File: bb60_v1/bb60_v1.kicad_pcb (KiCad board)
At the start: 2 copper layers, 141 parts, among them J1 Conn_01x04, SW1 SW_Push, SW2 SW_Push, U1 STM32F072CBTx, U2 XC6206PxxxMR, U3 USBLC6-2SC6

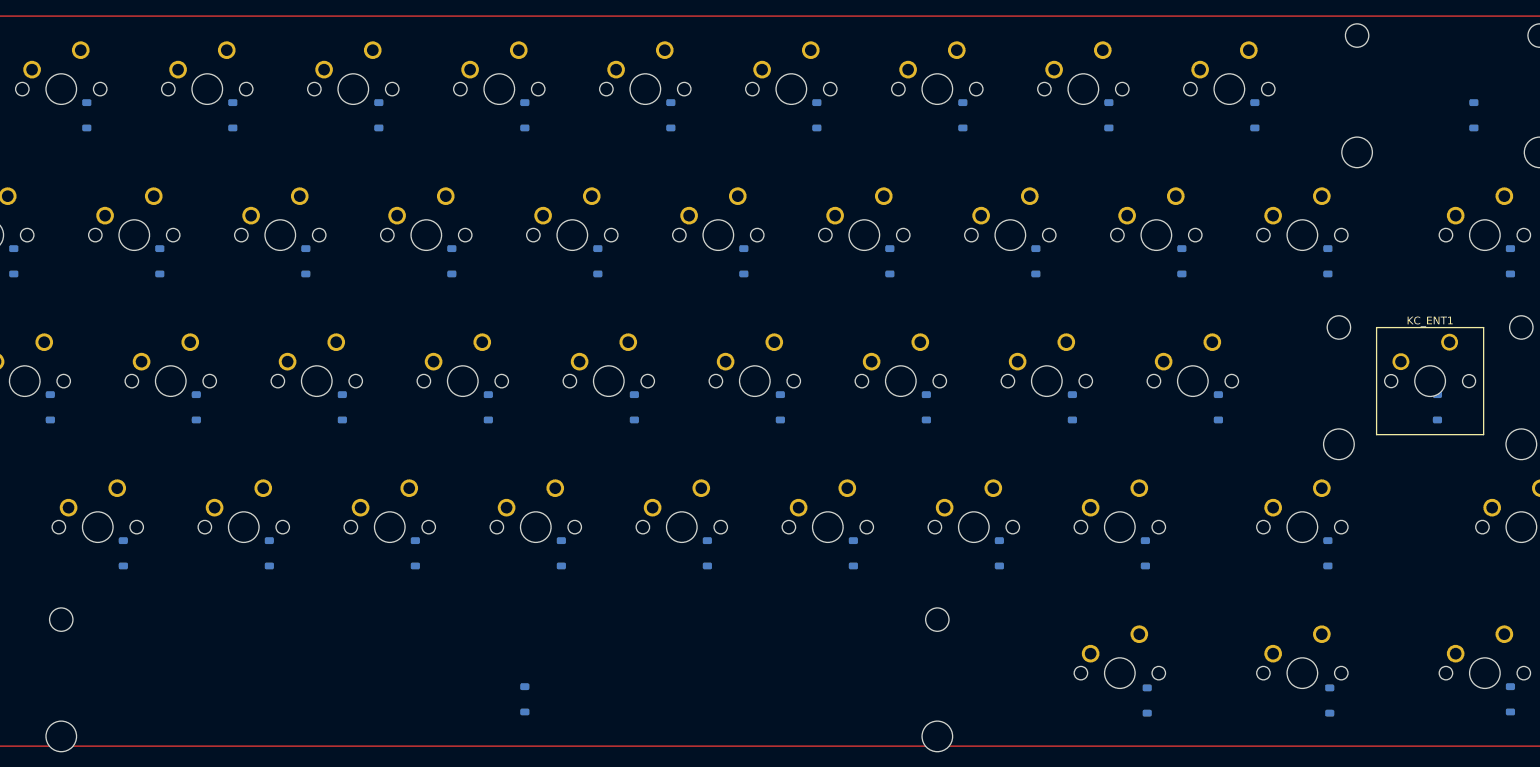
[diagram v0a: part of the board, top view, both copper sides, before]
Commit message: Fixed stab keys on pcb
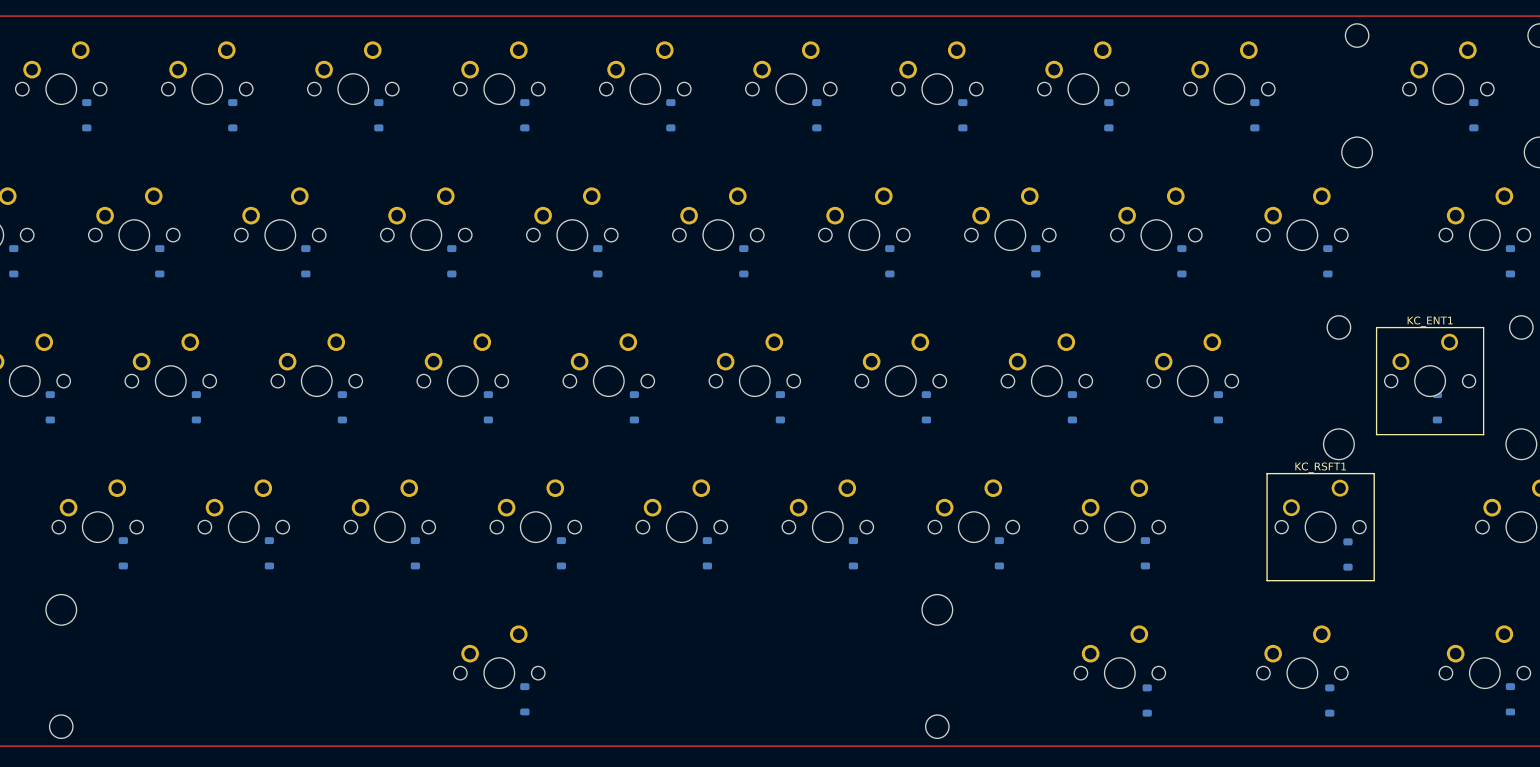
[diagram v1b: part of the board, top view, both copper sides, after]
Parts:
- added REF**: STAB_MX_7u, marbastlib-mx:STAB_MX_7u, F.Cu at (131.0, 145.3)
- added REF**: STAB_MX_2u, marbastlib-mx:STAB_MX_2u, F.Cu at (254.8, 69.1)
- KC_BKSP1: footprint marbastlib-mx:STAB_MX_2u -> marbastlib-mx:SW_MX_1u
- KC_RSFT1: footprint marbastlib-mx:SW_MX_1u -> Button_Switch_Keyboard:SW_Cherry_MX_1.75u_PCB
- KC_SPC1: footprint marbastlib-mx:STAB_MX_7u -> marbastlib-mx:SW_MX_1u
- moved KC_RSFT1 7.07 mm to (240.7, 121.1)
- moved D54 2.62 mm to (241.7, 129.8)

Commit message: Added row/column traces
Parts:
- moved D41 124.1 mm to (342.9, 196.5)
- moved D51 122.4 mm to (264.3, 215.5)
- moved D34 122.4 mm to (197.6, 196.5)
- moved D40 122.4 mm to (311.9, 196.5)
- moved KC_C1 122.4 mm to (165.7, 212.1)
- moved KC_DOT1 122.4 mm to (280.0, 212.1)
- moved KC_LBRC1 122.4 mm to (303.8, 174.0)
- moved KC_T1 122.4 mm to (189.5, 174.0)
- moved D19 122.4 mm to (173.8, 177.4)
- moved D25 122.4 mm to (288.1, 177.4)
- moved KC_3 122.4 mm to (141.9, 154.9)
- moved KC_9 122.4 mm to (256.2, 154.9)
- moved KC_H1 122.4 mm to (213.4, 193.0)
- moved KC_RSFT1 122.4 mm to (327.8, 207.0)
- moved C5 122.4 mm to (63.4, 170.9)
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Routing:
- net /ROW0: track 0.00 -> 338.7 mm
- net /ROW4: track 0.00 -> 338.2 mm
- net /ROW3: track 0.00 -> 317.4 mm
- net /ROW1: track 0.00 -> 261.8 mm, vias 0 -> 2
- net /ROW2: track 0.00 -> 257.8 mm, vias 0 -> 2
- net /COL6: track 0.00 -> 95.1 mm
- net /COL2: track 0.00 -> 91.7 mm
- net /COL11: track 0.00 -> 88.0 mm
- net /COL1: track 0.00 -> 85.1 mm
- net /COL13: track 0.00 -> 83.1 mm
- net /COL4: track 0.00 -> 68.7 mm
- net /COL8: track 0.00 -> 68.2 mm
- net /COL5: track 0.00 -> 68.0 mm
- net /COL7: track 0.00 -> 68.0 mm
- net /COL10: track 0.00 -> 68.0 mm
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
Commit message: Added Ai03 Library, fixed stab positions
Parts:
- added REF**: STAB_MX_P_2.25u, marbastlib-mx:STAB_MX_P_2.25u, F.Cu at (102.4, 202.2)
- added REF**: STAB_MX_P_2.25u, marbastlib-mx:STAB_MX_P_2.25u, F.Cu at (345.3, 183.2)
- KC_ENT1, KC_LSFT1: footprint Button_Switch_Keyboard:SW_Cherry_MX_2.25u_PCB -> marbastlib-mx:SW_MX_1u
- KC_RSFT1: footprint Button_Switch_Keyboard:SW_Cherry_MX_1.75u_PCB -> marbastlib-mx:SW_MX_1u
- moved D10 11.4 mm to (265.3, 148.5)
- moved D11 11.4 mm to (284.3, 148.5)
- moved D26 11.4 mm to (312.9, 167.6)
- moved D27 11.4 mm to (331.9, 167.6)
- moved D28 11.4 mm to (355.8, 167.6)
- moved D37 11.4 mm to (260.5, 186.6)
- moved D41 11.4 mm to (348.6, 186.6)
- moved D52 11.4 mm to (289.1, 205.7)
- moved D53 11.4 mm to (308.1, 205.7)
- moved D55 11.4 mm to (360.5, 205.7)
- moved D60 11.4 mm to (308.1, 224.7)
- moved D61 11.4 mm to (331.9, 224.7)
- moved D62 11.4 mm to (355.8, 224.7)
- moved KC_0 11.4 mm to (281.0, 145.1)
- moved KC_BKSP1 11.4 mm to (347.7, 145.1)
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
